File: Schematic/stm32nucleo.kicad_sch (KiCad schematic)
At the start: 0 parts

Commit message: add nucleo to schematic
Just add the nucleo to the schematic
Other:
- added sheet Part A (Part_A.kicad_sch)
- added sheet Part B (Part_B.kicad_sch)
- added sheet Part C (Part_C.kicad_sch)
- added sheet Part D (Part_D.kicad_sch)
- added sheet Part E (Part E.kicad_sch)
- added sheet Part F (Part_F.kicad_sch)
- added sheet Part G (Part_G.kicad_sch)
- added sheet Part H (Part_H.kicad_sch)
- added sheet Part I (Part_I.kicad_sch)
- added sheet Part J (Part_J.kicad_sch)

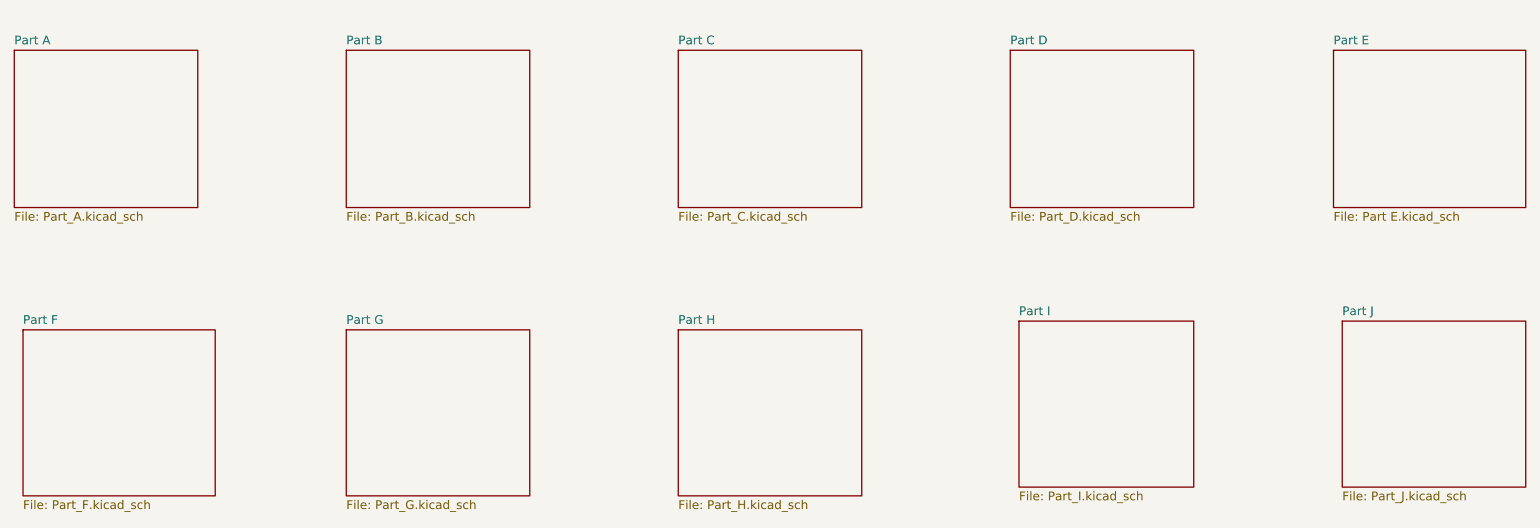
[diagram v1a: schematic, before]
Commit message: fix schematic and pcb layout
Fix Potentiometer errors, and updated schematic
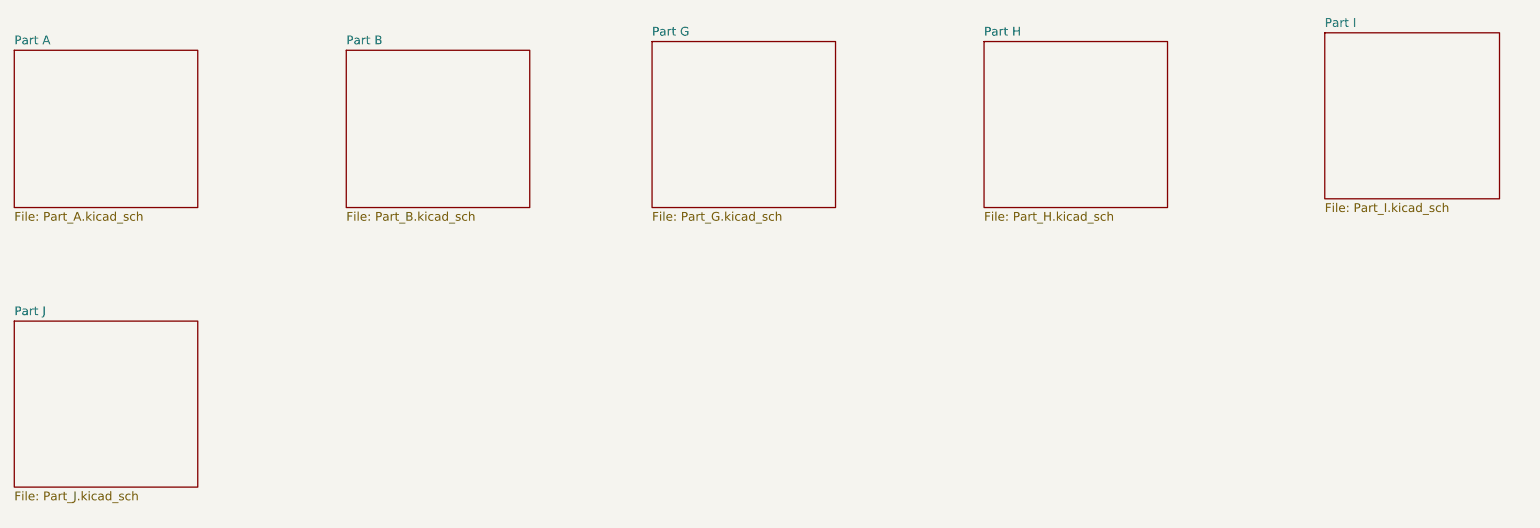
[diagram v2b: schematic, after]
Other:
- removed sheet Part C
- removed sheet Part D
- removed sheet Part E
- removed sheet Part F
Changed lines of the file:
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@@
 	)
 	(sheet
-		(at 86.36 72.39)
+		(at 130.81 30.48)
 		(size 26.67 24.13)
 		(exclude_from_sim no)
@@
 		)
 		(property "Sheetname" "Part G"
-			(at 86.36 71.6784 0)
+			(at 130.81 29.7684 0)
 			(effects
 				(font
@@
 		)
 		(property "Sheetfile" "Part_G.kicad_sch"
-			(at 86.36 97.1046 0)
+			(at 130.81 55.1946 0)
 			(effects
 				(font
@@
 	)
 	(sheet
-		(at 184.15 71.12)
+		(at 228.6 29.21)
 		(size 25.4 24.13)
 		(exclude_from_sim no)
@@
 		)
 		(property "Sheetname" "Part I"
-			(at 184.15 70.4084 0)
+			(at 228.6 28.4984 0)
 			(effects
 				(font
@@
 		)
 		(property "Sheetfile" "Part_I.kicad_sch"
-			(at 184.15 95.8346 0)
+			(at 228.6 53.9246 0)
 			(effects
 				(font
@@
 	)
 	(sheet
-		(at 231.14 71.12)
+		(at 38.1 71.12)
 		(size 26.67 24.13)
 		(exclude_from_sim no)
@@
 		)
 		(property "Sheetname" "Part J"
-			(at 231.14 70.4084 0)
+			(at 38.1 70.4084 0)
 			(effects
 				(font
@@
 		)
 		(property "Sheetfile" "Part_J.kicad_sch"
-			(at 231.14 95.8346 0)
+			(at 38.1 95.8346 0)
 			(effects
 				(font
@@
 	)
 	(sheet
-		(at 182.88 31.75)
-		(size 26.67 22.86)
-		(exclude_from_sim no)
-		(in_bom yes)
-		(on_board yes)
-		(dnp no)
-		(fields_autoplaced yes)
-		(stroke
-			(width 0.1524)
-			(type solid)
-		)
-		(fill
-			(color 0 0 0 0.0000)
-		)
-		(property "Sheetname" "Part D"
-			(at 182.88 31.0384 0)
-			(effects
-				(font
-					(size 1.27 1.27)
-				)
-				(justify left bottom)
-			)
-		)
-		(property "Sheetfile" "Part_D.kicad_sch"
-			(at 182.88 55.1946 0)
-			(effects
-				(font
-					(size 1.27 1.27)
-				)
-				(justify left top)
-			)
-		)
-		(instances
-			(project "Schematic"
-				(path "/e489aebc-5c18-43ce-b37f-71b1d4c7067c/65ad64f0-96b7-42ef-9c59-729e545063c1"
-					(page "7")
-				)
-			)
-		)
-	)
-	(sheet
-		(at 134.62 72.39)
+		(at 179.07 30.48)
 		(size 26.67 24.13)
 		(exclude_from_sim no)
@@
 		)
 		(property "Sheetname" "Part H"
-			(at 134.62 71.6784 0)
+			(at 179.07 29.7684 0)
 			(effects
 				(font
@@
 		)
 		(property "Sheetfile" "Part_H.kicad_sch"
-			(at 134.62 97.1046 0)
+			(at 179.07 55.1946 0)
 			(effects
 				(font
@@
 				(path "/e489aebc-5c18-43ce-b37f-71b1d4c7067c/65ad64f0-96b7-42ef-9c59-729e545063c1"
 					(page "11")
-				)
-			)
-		)
-	)
-	(sheet
-		(at 39.37 72.39)
-		(size 27.94 24.13)
-		(exclude_from_sim no)
-		(in_bom yes)
-		(on_board yes)
-		(dnp no)
-		(fields_autoplaced yes)
-		(stroke
-			(width 0.1524)
-			(type solid)
-		)
-		(fill
-			(color 0 0 0 0.0000)
-		)
-		(property "Sheetname" "Part F"
-			(at 39.37 71.6784 0)
-			(effects
-				(font
-					(size 1.27 1.27)
-				)
-				(justify left bottom)
-			)
-		)
-		(property "Sheetfile" "Part_F.kicad_sch"
-			(at 39.37 97.1046 0)
-			(effects
-				(font
-					(size 1.27 1.27)
-				)
-				(justify left top)
-			)
-		)
-		(instances
-			(project "Schematic"
-				(path "/e489aebc-5c18-43ce-b37f-71b1d4c7067c/65ad64f0-96b7-42ef-9c59-729e545063c1"
-					(page "9")
-				)
-			)
-		)
-	)
-	(sheet
-		(at 134.62 31.75)
-		(size 26.67 22.86)
-		(exclude_from_sim no)
-		(in_bom yes)
-		(on_board yes)
-		(dnp no)
-		(fields_autoplaced yes)
-		(stroke
-			(width 0.1524)
-			(type solid)
-		)
-		(fill
-			(color 0 0 0 0.0000)
-		)
-		(property "Sheetname" "Part C"
-			(at 134.62 31.0384 0)
-			(effects
-				(font
-					(size 1.27 1.27)
-				)
-				(justify left bottom)
-			)
-		)
-		(property "Sheetfile" "Part_C.kicad_sch"
-			(at 134.62 55.1946 0)
-			(effects
-				(font
-					(size 1.27 1.27)
-				)
-				(justify left top)
-			)
-		)
-		(instances
-			(project "Schematic"
-				(path "/e489aebc-5c18-43ce-b37f-71b1d4c7067c/65ad64f0-96b7-42ef-9c59-729e545063c1"
-					(page "6")
 				)
 			)
@@
 				)
 			)
-		)
-	)
-	(sheet
-		(at 229.87 31.75)
-		(size 27.94 22.86)
-		(exclude_from_sim no)
-		(in_bom yes)
-		(on_board yes)
-		(dnp no)
-		(fields_autoplaced yes)
-		(stroke
-			(width 0.1524)
-			(type solid)
-		)
-		(fill
-			(color 0 0 0 0.0000)
-		)
-		(property "Sheetname" "Part E"
-			(at 229.87 31.0384 0)
-			(effects
-				(font
-					(size 1.27 1.27)
-				)
-				(justify left bottom)
-			)
-		)
-		(property "Sheetfile" "Part E.kicad_sch"
-			(at 229.87 55.1946 0)
-			(effects
-				(font
-					(size 1.27 1.27)
-				)
-				(justify left top)
-			)
-		)
-		(instances
-			(project "Schematic"
-				(path "/e489aebc-5c18-43ce-b37f-71b1d4c7067c/65ad64f0-96b7-42ef-9c59-729e545063c1"
-					(page "8")
-				)
-			)
